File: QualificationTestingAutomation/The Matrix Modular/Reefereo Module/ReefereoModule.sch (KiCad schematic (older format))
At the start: 0 parts

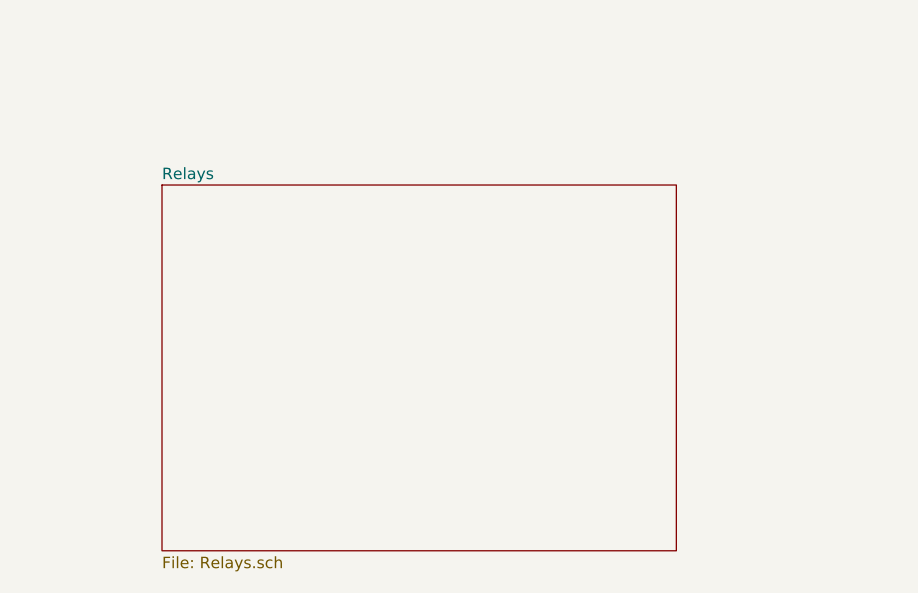
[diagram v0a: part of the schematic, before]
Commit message: Reefero Module PCB design
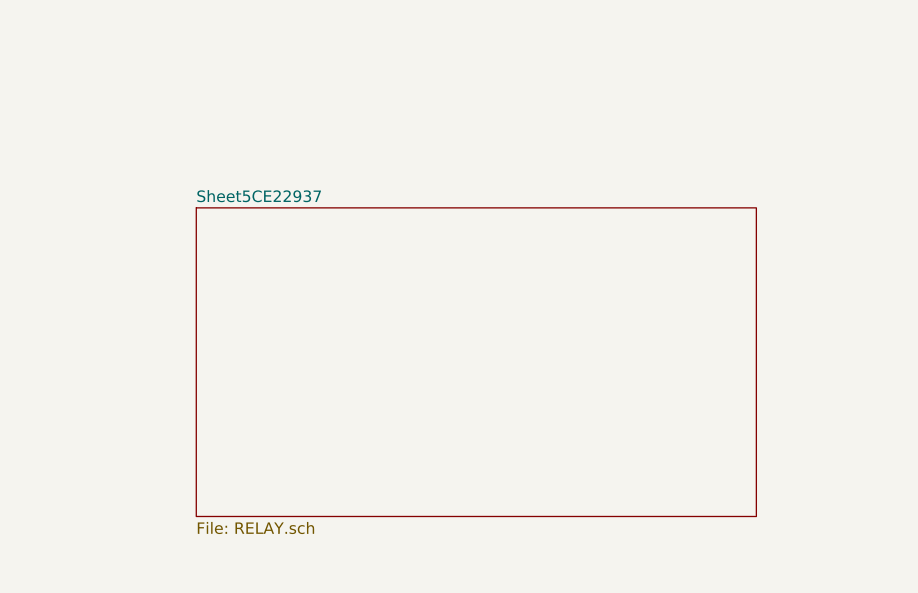
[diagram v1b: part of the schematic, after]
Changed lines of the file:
@@
 EESchema Schematic File Version 4
 LIBS:ReefereoModule-cache
-EELAYER 26 0
+EELAYER 29 0
 EELAYER END
 $Descr A4 11693 8268
@@
 $EndSheet
 $Sheet
-S 4200 4350 2250 1600
-U 5C8DF48C
-F0 "Relays" 50
-F1 "Relays.sch" 50
-$EndSheet
-$Sheet
 S 1250 4400 2050 1450
 U 5C90F517
@@
 F1 "ADE7758.sch" 50
 $EndSheet
+$Sheet
+S 4350 4450 2450 1350
+U 5CE22938
+F0 "Sheet5CE22937" 50
+F1 "RELAY.sch" 50
+$EndSheet
 $EndSCHEMATC
